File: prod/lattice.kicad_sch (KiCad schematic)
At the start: 69 parts, among them J1 USB_C_Receptacle, J2 USB_C_Receptacle, SW1 SW_Slide_DPDT, SW2 SW_Slide_DPDT, SW3 SW_Slide_DPDT, U1 CH552T, U2 USBLC6-2SC6

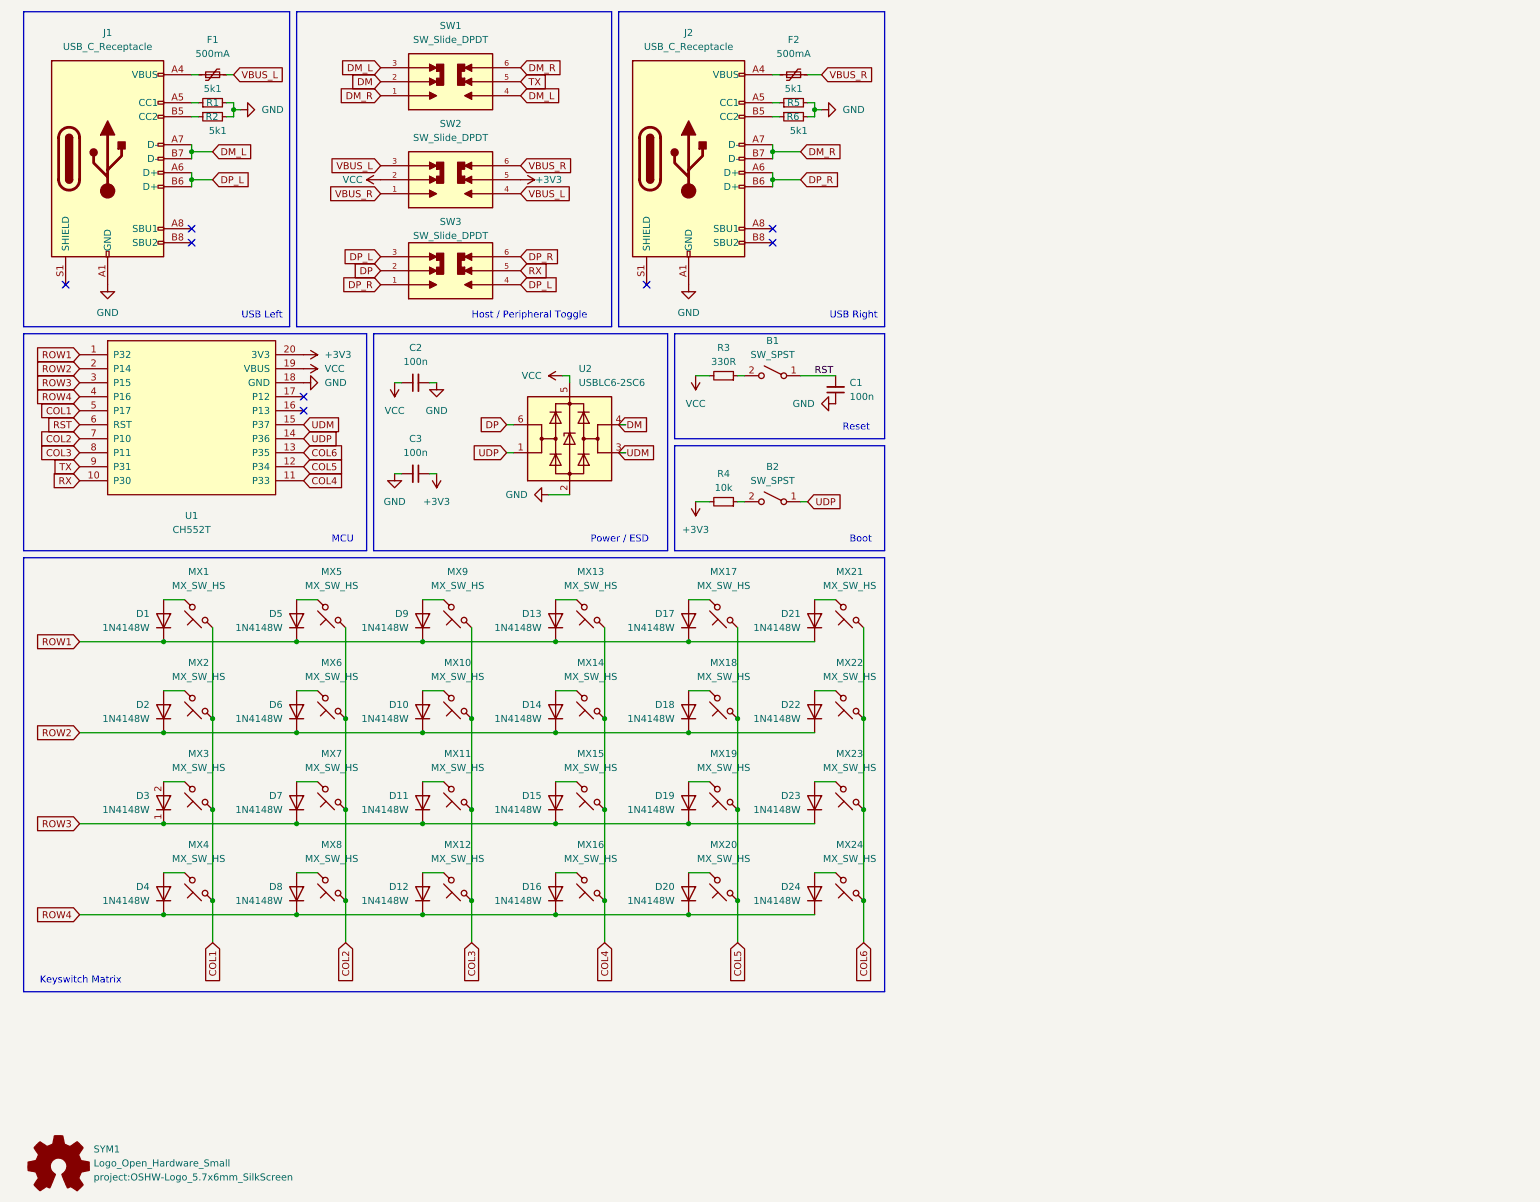
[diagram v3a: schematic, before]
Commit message: 4 channel mux/demux
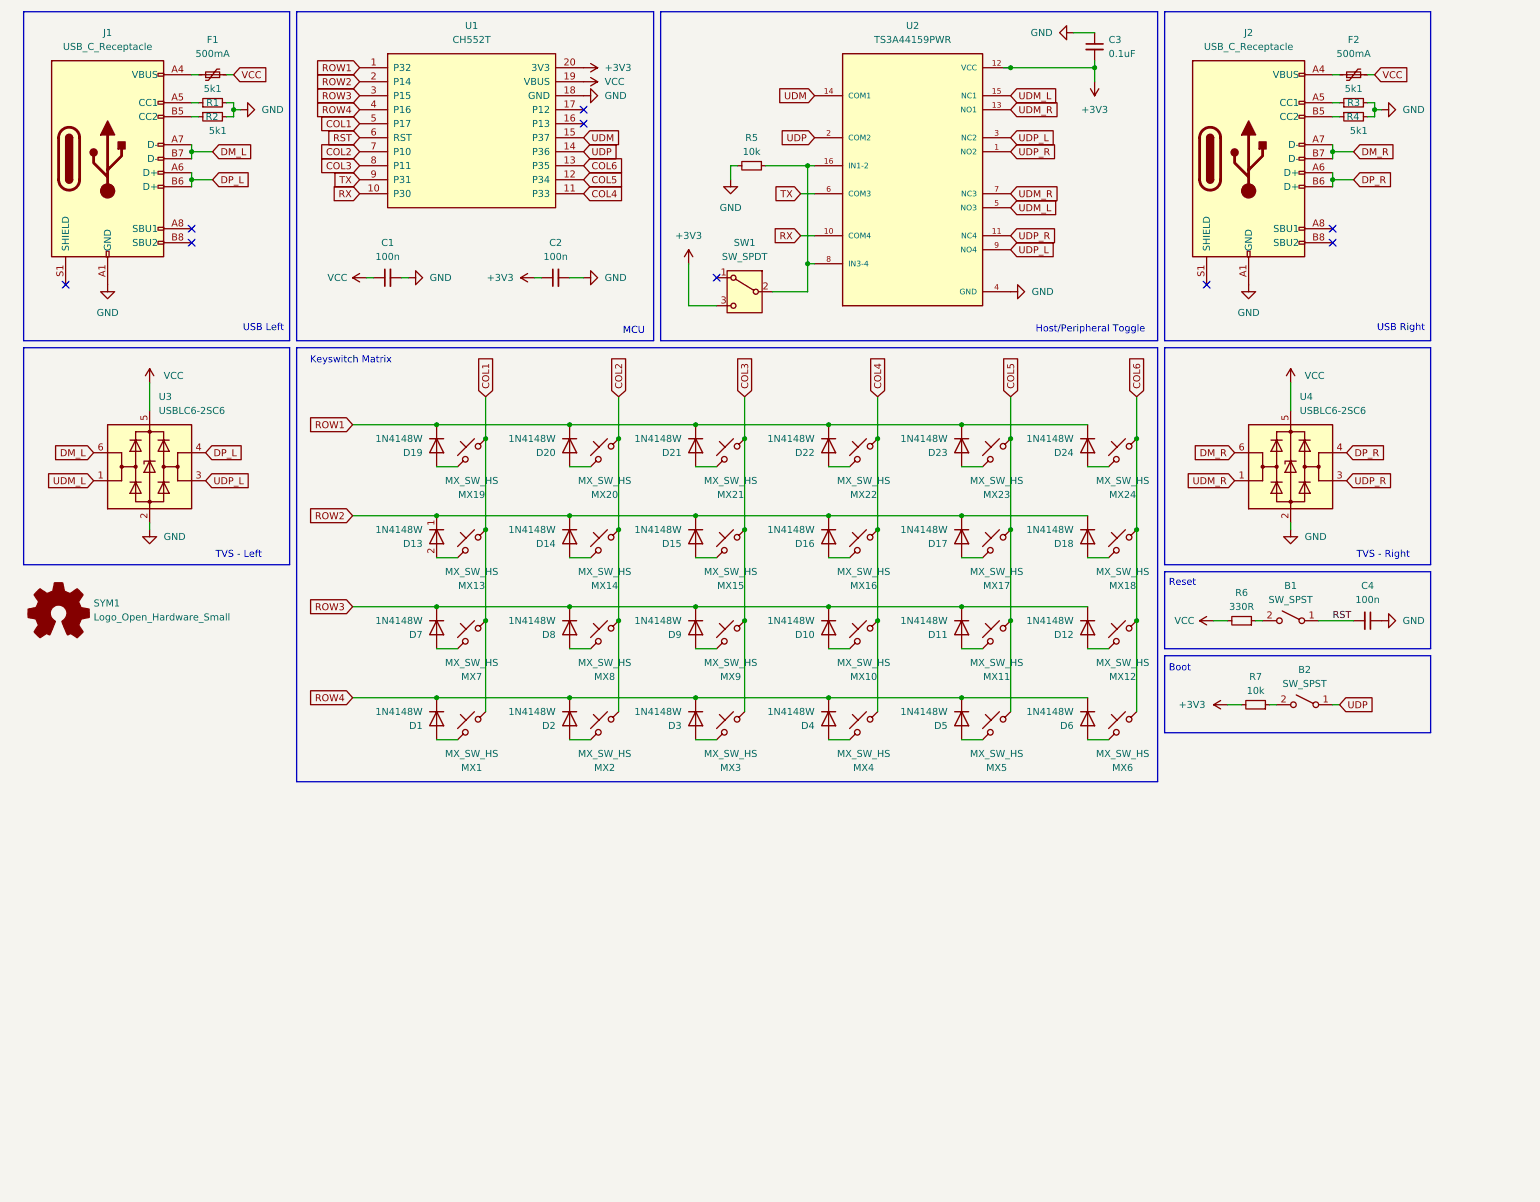
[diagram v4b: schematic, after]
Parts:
- removed R6: 5k1, project:R_0603_1608Metric, symbol lattice:R_Small
- removed SW1, SW2, SW3: SW_Slide_DPDT, project:K3_1390S, symbol lattice:SW_Slide_DPDT
- added C3: 0.1uF, project:C_0603_1608Metric, symbol lattice:C_Small
- added R3, R4: 5k1, project:R_0603_1608Metric, symbol lattice:R_Small
- added SW1: SW_SPDT, Button_Switch_SMD:SW_SPDT_PCM12, symbol lattice:SW_SPDT
- added U2: TS3A44159PWR, Package_SO:TSSOP-16_4.4x5mm_P0.65mm, symbol lattice:TS3A44159PWR
- added U4: USBLC6-2SC6, project:SOT-23-6, symbol lattice:USBLC6-2SC6
- R5: value 5k1 -> 10k
- renumbered C2 to C1, C3 to C2, C1 to C4, D14 to D10, D18 to D11, D22 to D12, D3 to D13, D7 to D14, D11 to D15, D15 to D16, D19 to D17, D23 to D18, D4 to D19, D5 to D2, D8 to D20, D12 to D21, D16 to D22, D20 to D23, D9 to D3, D13 to D4, D17 to D5, D21 to D6, D2 to D7, D6 to D8, D10 to D9, MX14 to MX10, MX18 to MX11, MX22 to MX12, MX3 to MX13, MX7 to MX14, MX11 to MX15, MX15 to MX16, MX19 to MX17, MX23 to MX18, MX4 to MX19, MX5 to MX2, MX8 to MX20, MX12 to MX21, MX16 to MX22, MX20 to MX23, MX9 to MX3, MX13 to MX4, MX17 to MX5, MX21 to MX6, MX2 to MX7, MX6 to MX8, MX10 to MX9, R3 to R6, R4 to R7, U2 to U3
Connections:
- net DM is gone; now on net DP_L: U3.4 (I/O2)
- net DP is gone; now on net DM_L: U3.6 (I/O1)
- net VBUS_L is gone; now on net VCC: F1.2
- net VBUS_R is gone; now on net VCC: F2.2
- net +3V3: now also C3.2, SW1.3 (C), U2.12 (VCC)
- net DM_R: now also U4.6 (I/O1)
- net DP_R: now also U4.4 (I/O2)
- net GND: now also C3.1, R3.2, R4.2, U2.4 (GND), U4.2 (GND)
- net ROW1: now also D19.1 (K), D20.1 (K), D21.1 (K), D22.1 (K), D23.1 (K), D24.1 (K); no longer D1.1 (K), D2.1 (K), D3.1 (K), D4.1 (K), D5.1 (K), D6.1 (K)
- net ROW2: now also D13.1 (K), D14.1 (K), D15.1 (K), D16.1 (K), D17.1 (K), D18.1 (K); no longer D10.1 (K), D11.1 (K), D12.1 (K), D7.1 (K), D8.1 (K), D9.1 (K)
- net ROW3: now also D10.1 (K), D11.1 (K), D12.1 (K), D7.1 (K), D8.1 (K), D9.1 (K); no longer D13.1 (K), D14.1 (K), D15.1 (K), D16.1 (K), D17.1 (K), D18.1 (K)
- net ROW4: now also D1.1 (K), D2.1 (K), D3.1 (K), D4.1 (K), D5.1 (K), D6.1 (K); no longer D19.1 (K), D20.1 (K), D21.1 (K), D22.1 (K), D23.1 (K), D24.1 (K)
- net RX: now also U2.10 (COM4)
- net TX: now also U2.6 (COM3)
- net UDM: now also U2.14 (COM1); no longer U3.3 (I/O2)
- net UDP: now also U2.2 (COM2); no longer U3.1 (I/O1)
- net VCC: now also U4.5 (VBUS)
- net at R5.1: now also SW1.2 (B), U2.16 (IN1-2), U2.8 (IN3-4); no longer J2.A5 (CC1)
- net at J2.B5 (CC2): now also R4.1
- new net: J2.A5 (CC1), R3.1
- new net UDM_L: U2.15 (NC1), U2.5 (NO3), U3.1 (I/O1)
- new net UDM_R: U2.13 (NO1), U2.7 (NC3), U4.1 (I/O1)
- new net UDP_L: U2.3 (NC2), U2.9 (NO4), U3.3 (I/O2)
- new net UDP_R: U2.1 (NO2), U2.11 (NC4), U4.3 (I/O2)
- no-connect marks 8 -> 9
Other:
- note added: "Host/Peripheral Toggle"
- note added: "TVS - Left"
- note added: "TVS - Right"
- note removed: "Host / Peripheral Toggle"
- note removed: "Power / ESD"
- moved on the sheet: B1, B2, C1, C2, C4, D1, D10, D11, D12, D13, D14, D15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

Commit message: CFX spacing, solder jumpers
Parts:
- removed B1: SW_SPST, project:SW_SPST_SKQG_WithStem, symbol lattice:SW_SPST
- removed C3: 0.1uF, project:C_0603_1608Metric, symbol lattice:C_Small
- removed C4: 100n, project:C_0603_1608Metric, symbol lattice:C_Small
- removed R5: 10k, project:R_0603_1608Metric, symbol lattice:R_Small
- removed R6: 330R, project:R_0603_1608Metric, symbol lattice:R_Small
- removed SW1: SW_SPDT, Button_Switch_SMD:SW_SPDT_PCM12, symbol lattice:SW_SPDT
- removed U2: TS3A44159PWR, Package_SO:TSSOP-16_4.4x5mm_P0.65mm, symbol lattice:TS3A44159PWR
- added JP1, JP2, JP3, JP4, JP5, JP6: SolderJumper_3_Open, project:SolderJumper-3_P1.3mm_Open_RoundedPad1.0x1.5mm, symbol Jumper:SolderJumper_3_Open
- B1: renamed from B2; value SW_SPST -> Pad_1x02; footprint project:SW_SPST_SKQG_WithStem -> project:Pad_1x02_P2.54mm_tht_boot
- C1, C2: footprint project:C_0603_1608Metric -> Capacitor_SMD:C_0805_2012Metric_Pad1.18x1.45mm_HandSolder
- F1, F2: footprint project:Fuse_0603_1608Metric -> Fuse:Fuse_0805_2012Metric_Pad1.15x1.40mm_HandSolder
- K1: renamed from MX1; value MX_SW_HS -> SW_choc_v1_1u; footprint project:SW_MX_HS_S_1u -> project:SW_choc_v1_1u
- K10: renamed from MX9; value MX_SW_HS -> SW_choc_v1_1u; footprint project:SW_MX_HS_S_1u -> project:SW_choc_v1_1u
- K11: renamed from MX15; value MX_SW_HS -> SW_choc_v1_1u; footprint project:SW_MX_HS_S_1u -> project:SW_choc_v1_1u
- K12: renamed from MX21; value MX_SW_HS -> SW_choc_v1_1u; footprint project:SW_MX_HS_S_1u -> project:SW_choc_v1_1u
- K13: renamed from MX4; value MX_SW_HS -> SW_choc_v1_1u; footprint project:SW_MX_HS_S_1u -> project:SW_choc_v1_1u
- K14: renamed from MX10; value MX_SW_HS -> SW_choc_v1_1u; footprint project:SW_MX_HS_S_1u -> project:SW_choc_v1_1u
- K15: renamed from MX16; value MX_SW_HS -> SW_choc_v1_1u; footprint project:SW_MX_HS_S_1u -> project:SW_choc_v1_1u
- K16: renamed from MX22; value MX_SW_HS -> SW_choc_v1_1u; footprint project:SW_MX_HS_S_1u -> project:SW_choc_v1_1u
- K17: renamed from MX5; value MX_SW_HS -> SW_choc_v1_1u; footprint project:SW_MX_HS_S_1u -> project:SW_choc_v1_1u
- K18: renamed from MX11; value MX_SW_HS -> SW_choc_v1_1u; footprint project:SW_MX_HS_S_1u -> project:SW_choc_v1_1u
- K19: renamed from MX17; value MX_SW_HS -> SW_choc_v1_1u; footprint project:SW_MX_HS_S_1u -> project:SW_choc_v1_1u
- K2: renamed from MX7; value MX_SW_HS -> SW_choc_v1_1u; footprint project:SW_MX_HS_S_1u -> project:SW_choc_v1_1u
- K20: renamed from MX23; value MX_SW_HS -> SW_choc_v1_1u; footprint project:SW_MX_HS_S_1u -> project:SW_choc_v1_1u
- K21: renamed from MX6; value MX_SW_HS -> SW_choc_v1_1u; footprint project:SW_MX_HS_S_1u -> project:SW_choc_v1_1u
- K22: renamed from MX12; value MX_SW_HS -> SW_choc_v1_1u; footprint project:SW_MX_HS_S_1u -> project:SW_choc_v1_1u
- K23: renamed from MX18; value MX_SW_HS -> SW_choc_v1_1u; footprint project:SW_MX_HS_S_1u -> project:SW_choc_v1_1u
- K24: renamed from MX24; value MX_SW_HS -> SW_choc_v1_1u; footprint project:SW_MX_HS_S_1u -> project:SW_choc_v1_1u
- K3: renamed from MX13; value MX_SW_HS -> SW_choc_v1_1u; footprint project:SW_MX_HS_S_1u -> project:SW_choc_v1_1u
- K4: renamed from MX19; value MX_SW_HS -> SW_choc_v1_1u; footprint project:SW_MX_HS_S_1u -> project:SW_choc_v1_1u
- K5: renamed from MX2; value MX_SW_HS -> SW_choc_v1_1u; footprint project:SW_MX_HS_S_1u -> project:SW_choc_v1_1u
- K6: renamed from MX8; value MX_SW_HS -> SW_choc_v1_1u; footprint project:SW_MX_HS_S_1u -> project:SW_choc_v1_1u
- K7: renamed from MX14; value MX_SW_HS -> SW_choc_v1_1u; footprint project:SW_MX_HS_S_1u -> project:SW_choc_v1_1u
- K8: renamed from MX20; value MX_SW_HS -> SW_choc_v1_1u; footprint project:SW_MX_HS_S_1u -> project:SW_choc_v1_1u
- K9: renamed from MX3; value MX_SW_HS -> SW_choc_v1_1u; footprint project:SW_MX_HS_S_1u -> project:SW_choc_v1_1u
- R1, R2, R3, R4: footprint project:R_0603_1608Metric -> Resistor_SMD:R_0805_2012Metric_Pad1.20x1.40mm_HandSolder
- R5: renamed from R7; footprint project:R_0603_1608Metric -> Resistor_SMD:R_0805_2012Metric_Pad1.20x1.40mm_HandSolder
- U2: renamed from U3; footprint project:SOT-23-6 -> Package_TO_SOT_SMD:SOT-23-6_Handsoldering
- U3: renamed from U4; footprint project:SOT-23-6 -> Package_TO_SOT_SMD:SOT-23-6_Handsoldering
- renumbered D9 to D10, D15 to D11, D21 to D12, D4 to D13, D10 to D14, D16 to D15, D22 to D16, D5 to D17, D11 to D18, D17 to D19, D7 to D2, D23 to D20, D6 to D21, D12 to D22, D18 to D23, D13 to D3, D19 to D4, D2 to D5, D8 to D6, D14 to D7, D20 to D8, D3 to D9
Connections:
- net RX: now also JP5.3 (B), JP6.1 (A)
- net TX: now also JP5.1 (A), JP6.3 (B)
- net UDM: now also JP1.2 (C)
- net UDM_L: now also JP1.1 (A), JP3.3 (B)
- net UDM_R: now also JP1.3 (B), JP3.1 (A)
- net UDP: now also JP2.2 (C)
- net UDP_L: now also JP2.1 (A), JP4.3 (B)
- net UDP_R: now also JP2.3 (B), JP4.1 (A)
- new net SERIAL0: JP3.2 (C), JP5.2 (C)
- new net SERIAL1: JP4.2 (C), JP6.2 (C)
- no-connect marks 9 -> 8
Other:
- note added: "Host"
- note added: "LHS: bridge 1 and 2 RHS: bridge 2 and 3"
- note added: "Peripheral"
- note added: "Serial comms (USART Full Duplex)"
- note removed: "Reset"
- moved on the sheet: B1, R5

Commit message: boot button, remove refereence designators, jumper labels
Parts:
- B1: value Pad_1x02 -> SW_SPST_SKQG; footprint project:Pad_1x02_P2.54mm_tht_boot -> project:SW_SPST_SKQG_WithStem
- C1, C2: footprint Capacitor_SMD:C_0805_2012Metric_Pad1.18x1.45mm_HandSolder -> project:C_0805_2012Metric_Pad1.18x1.45mm_HandSolder
- F1, F2: footprint Fuse:Fuse_0805_2012Metric_Pad1.15x1.40mm_HandSolder -> project:Fuse_0805_2012Metric_Pad1.15x1.40mm_HandSolder
- JP1, JP2, JP3, JP4, JP5, JP6: symbol Jumper:SolderJumper_3_Open -> lattice:SolderJumper_3_Open
- R1, R2, R3, R4, R5: footprint Resistor_SMD:R_0805_2012Metric_Pad1.20x1.40mm_HandSolder -> project:R_0805_2012Metric_Pad1.20x1.40mm_HandSolder
- U2, U3: footprint Package_TO_SOT_SMD:SOT-23-6_Handsoldering -> project:SOT-23-6_Handsoldering
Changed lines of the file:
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@@
 			)
 		)
-		(property "Footprint" "Fuse:Fuse_0805_2012Metric_Pad1.15x1.40mm_HandSolder"
+		(property "Footprint" "project:Fuse_0805_2012Metric_Pad1.15x1.40mm_HandSolder"
 			(at 259.08 22.86 0)
 			(effects
@@
 	)
 	(symbol
-		(lib_id "Jumper:SolderJumper_3_Open")
+		(lib_id "lattice:SolderJumper_3_Open")
 		(at 207.01 26.67 270)
 		(unit 1)
@@
 	)
 	(symbol
-		(lib_id "Jumper:SolderJumper_3_Open")
+		(lib_id "lattice:SolderJumper_3_Open")
 		(at 147.32 27.94 270)
 		(unit 1)
@@
 	)
 	(symbol
-		(lib_id "Jumper:SolderJumper_3_Open")
+		(lib_id "lattice:SolderJumper_3_Open")
 		(at 166.37 27.94 270)
 		(unit 1)
@@
 			)
 		)
-		(property "Footprint" "Resistor_SMD:R_0805_2012Metric_Pad1.20x1.40mm_HandSolder"
+		(property "Footprint" "project:R_0805_2012Metric_Pad1.20x1.40mm_HandSolder"
 			(at 46.99 29.21 0)
 			(effects
@@
 			)
 		)
-		(property "Footprint" "Fuse:Fuse_0805_2012Metric_Pad1.15x1.40mm_HandSolder"
+		(property "Footprint" "project:Fuse_0805_2012Metric_Pad1.15x1.40mm_HandSolder"
 			(at 52.07 22.86 0)
 			(effects
@@
 			)
 		)
-		(property "Footprint" "Package_TO_SOT_SMD:SOT-23-6_Handsoldering"
+		(property "Footprint" "project:SOT-23-6_Handsoldering"
 			(at 35.56 107.95 0)
 			(effects
@@
 			)
 		)
-		(property "Footprint" "Resistor_SMD:R_0805_2012Metric_Pad1.20x1.40mm_HandSolder"
+		(property "Footprint" "project:R_0805_2012Metric_Pad1.20x1.40mm_HandSolder"
 			(at 46.99 31.75 0)
 			(effects
@@
 	)
 	(symbol
-		(lib_id "Jumper:SolderJumper_3_Open")
+		(lib_id "lattice:SolderJumper_3_Open")
 		(at 135.89 27.94 270)
 		(unit 1)
@@
 	)
 	(symbol
-		(lib_id "Jumper:SolderJumper_3_Open")
+		(lib_id "lattice:SolderJumper_3_Open")
 		(at 177.8 27.94 270)
 		(unit 1)
@@
 			)
 		)
-		(property "Footprint" "Capacitor_SMD:C_0805_2012Metric_Pad1.18x1.45mm_HandSolder"
+		(property "Footprint" "project:C_0805_2012Metric_Pad1.18x1.45mm_HandSolder"
 			(at 109.22 60.96 0)
 			(effects
@@
 			)
 		)
-		(property "Footprint" "Capacitor_SMD:C_0805_2012Metric_Pad1.18x1.45mm_HandSolder"
+		(property "Footprint" "project:C_0805_2012Metric_Pad1.18x1.45mm_HandSolder"
 			(at 78.74 60.96 0)
 			(effects
@@
 			)
 		)
-		(property "Footprint" "Resistor_SMD:R_0805_2012Metric_Pad1.20x1.40mm_HandSolder"
+		(property "Footprint" "project:R_0805_2012Metric_Pad1.20x1.40mm_HandSolder"
 			(at 254 31.75 0)
 			(effects
@@
 			)
 		)
-		(property "Footprint" "Resistor_SMD:R_0805_2012Metric_Pad1.20x1.40mm_HandSolder"
+		(property "Footprint" "project:R_0805_2012Metric_Pad1.20x1.40mm_HandSolder"
 			(at 254 29.21 0)
 			(effects
@@
 			)
 		)
-		(property "Value" "Pad_1x02"
+		(property "Value" "SW_SPST_SKQG"
 			(at 245.11 119.38 0)
 			(effects
@@
 			)
 		)
-		(property "Footprint" "project:Pad_1x02_P2.54mm_tht_boot"
+		(property "Footprint" "project:SW_SPST_SKQG_WithStem"
 			(at 245.11 123.19 0)
 			(effects
@@
 	)
 	(symbol
-		(lib_id "Jumper:SolderJumper_3_Open")
+		(lib_id "lattice:SolderJumper_3_Open")
 		(at 194.31 26.67 270)
 		(unit 1)
@@
 			)
 		)
-		(property "Footprint" "Package_TO_SOT_SMD:SOT-23-6_Handsoldering"
+		(property "Footprint" "project:SOT-23-6_Handsoldering"
 			(at 242.57 107.95 0)
 			(effects
@@
 			)
 		)
-		(property "Footprint" "Resistor_SMD:R_0805_2012Metric_Pad1.20x1.40mm_HandSolder"
+		(property "Footprint" "project:R_0805_2012Metric_Pad1.20x1.40mm_HandSolder"
 			(at 236.22 123.19 0)
 			(effects

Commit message: jumper label as footprint
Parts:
- added L1: SolderJumperLabel, project:JumperLabels, symbol lattice:SolderJumperLabel
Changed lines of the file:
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@@
+	)
+	(symbol
+		(lib_id "lattice:SolderJumperLabel")
+		(at 195.58 57.15 0)
+		(unit 1)
+		(exclude_from_sim no)
+		(in_bom yes)
+		(on_board yes)
+		(dnp no)
+		(fields_autoplaced yes)
+		(property "Reference" "L1"
+			(at 196.85 55.8799 0)
+			(effects
+				(font
+					(size 1.27 1.27)
+				)
+				(justify left)
+			)
+		)
+		(property "Value" "SolderJumperLabel"
+			(at 196.85 58.4199 0)
+			(effects
+				(font
+					(size 1.27 1.27)
+				)
+				(justify left)
+			)
+		)
+		(property "Footprint" "project:JumperLabels"
+			(at 195.58 57.15 0)
+			(effects
+				(font
+					(size 1.27 1.27)
+				)
+				(hide yes)
+			)
+		)
+		(property "Datasheet" ""
+			(at 195.58 57.15 0)
+			(effects
+				(font
+					(size 1.27 1.27)
+				)
+				(hide yes)
+			)
+		)
+		(property "Description" ""
+			(at 195.58 57.15 0)
+			(effects
+				(font
+					(size 1.27 1.27)
+				)
+				(hide yes)
+			)
+		)
+		(instances
+			(project "lattice"
+				(path "/7175bad1-6d67-4925-85bf-3e5286dbd285"
+					(reference "L1")
+					(unit 1)
+				)
+			)
+		)
 	)
 	(symbol
